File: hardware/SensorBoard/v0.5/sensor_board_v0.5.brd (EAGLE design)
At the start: 46.8 x 39.9 mm, 58 parts, among them J3 USB-MICROB, U1 ATMEGA328P, U2 TSL2561, U4 MPL115A, U5 FT231XS, U6 ADMP401, U7 SHT31-DIS, U8 MCP1703CB, U9 MCP1703CB, Y1 16MHZ

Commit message: Added extra GND vias
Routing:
- net GND: track 76.5 -> 73.8 mm, vias 19 -> 24
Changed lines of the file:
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@@
 </element>
 <element name="C14" library="SparkFun-Passives" package="0805" value="0.1uF" x="32.4612" y="44.1706" smashed="yes">
-<attribute name="VALUE" x="32.1056" y="45.1612" size="0.508" layer="121" font="vector"/>
+<attribute name="VALUE" x="31.496" y="42.8244" size="0.508" layer="121" font="vector"/>
 </element>
 <element name="MICS4514" library="MICS-4514_CO_and_NOx_Sensor_Breakout" package="SPARKFUN-SENSORS_MICS_10-SMD" value="SPARKFUN-SENSORS_MICS-4514" x="28.6512" y="26.4414" smashed="yes" rot="R90">
@@
 <attribute name="MPN" value="" x="27.178" y="44.6024" size="1.778" layer="27" rot="R180" display="off"/>
 <attribute name="OC_NEWARK" value="unknown" x="27.178" y="44.6024" size="1.778" layer="27" rot="R180" display="off"/>
-<attribute name="VALUE" x="28.194" y="43.6626" size="0.508" layer="121" font="vector" rot="R180"/>
+<attribute name="VALUE" x="28.2448" y="43.6626" size="0.508" layer="121" font="vector" rot="R180"/>
 </element>
 <element name="U$4" library="RFM69 USB Gateway" package="LOWPOWERLAB_RFM69W-MINPADS" value="RFM69HW" x="28.8036" y="37.0332" smashed="yes" rot="MR180">
@@
 <wire x1="23.6728" y1="45.0464" x2="23.6596" y2="45.0596" width="0.1778" layer="1"/>
 <wire x1="15.6464" y1="45.0464" x2="15.6464" y2="44.3484" width="0.1778" layer="1"/>
-<wire x1="15.6464" y1="44.3484" x2="17.5768" y2="42.418" width="0.1778" layer="1"/>
 <wire x1="17.5768" y1="42.418" x2="18.3512" y2="42.418" width="0.1778" layer="1"/>
 <wire x1="18.3512" y1="42.418" x2="18.3596" y2="42.4096" width="0.1778" layer="1"/>
@@
 <via x="31.5468" y="42.2148" extent="1-16" drill="0.254" diameter="0.127"/>
 <via x="34.4932" y="45.1612" extent="1-16" drill="0.254" diameter="0.127"/>
-<via x="47.0916" y="44.7548" extent="1-16" drill="0.254" diameter="0.127"/>
+<via x="16.6624" y="42.3672" extent="1-16" drill="0.254" diameter="0.127"/>
 <wire x1="45.2562" y1="28.8504" x2="46.9432" y2="28.8504" width="0.1778" layer="1"/>
 <wire x1="46.9432" y1="28.8504" x2="46.4312" y2="28.6004" width="0.1778" layer="1"/>
@@
 <via x="44.5516" y="33.1978" extent="1-16" drill="0.254" diameter="0.127"/>
 <via x="43.688" y="30.6578" extent="1-16" drill="0.254" diameter="0.127"/>
+<via x="49.9872" y="22.1996" extent="1-16" drill="0.254" diameter="0.127"/>
+<via x="11.938" y="27.3812" extent="1-16" drill="0.254" diameter="0.127"/>
+<via x="29.0576" y="12.5984" extent="1-16" drill="0.254" diameter="0.127"/>
+<via x="32.258" y="23.5204" extent="1-16" drill="0.254" diameter="0.127"/>
+<via x="51.054" y="38.7096" extent="1-16" drill="0.254" diameter="0.127"/>
 </signal>
 <signal name="VCC">

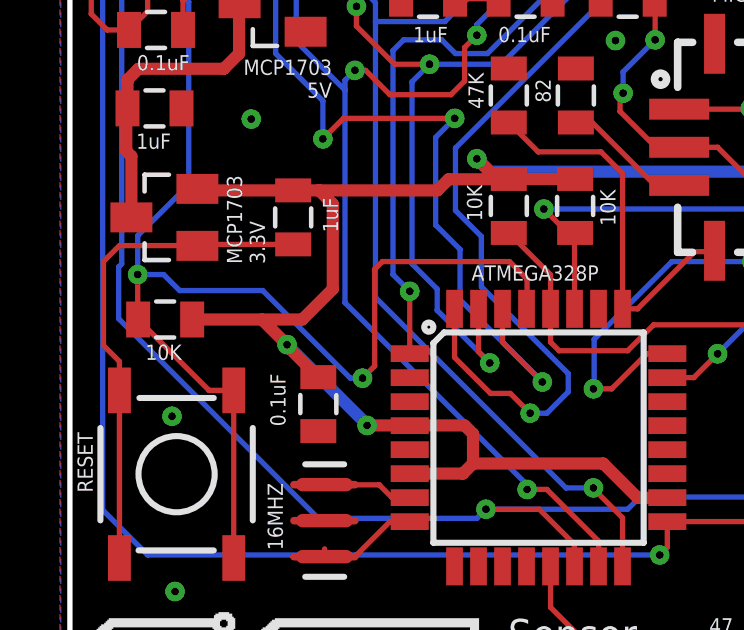
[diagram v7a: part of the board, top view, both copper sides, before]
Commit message: Adjusted some traces around MCU
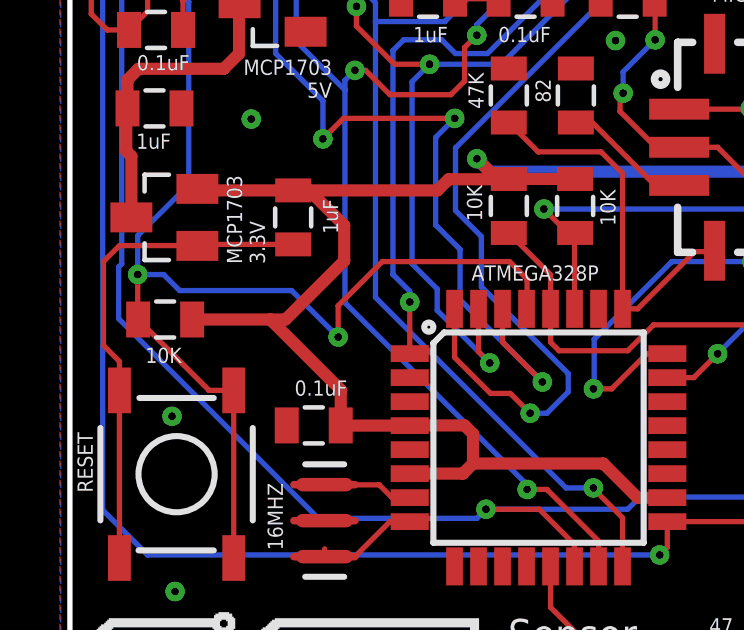
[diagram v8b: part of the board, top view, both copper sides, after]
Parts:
- moved C15 0.73 mm to (14.0, 17.2), turned to 180 degrees
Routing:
- net VCC: track 151.4 -> 148.1 mm, vias 7 -> 5
- net RESET: track 54.9 -> 52.5 mm
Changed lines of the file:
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@@
 <attribute name="MF" value="" x="13.335" y="24.1046" size="1.778" layer="27" rot="R270" display="off"/>
 <attribute name="MPN" value="" x="13.335" y="24.1046" size="1.778" layer="27" rot="R270" display="off"/>
-<attribute name="VALUE" x="14.3256" y="24.765" size="0.508" layer="121" font="vector" rot="R270"/>
+<attribute name="VALUE" x="14.3256" y="24.7142" size="0.508" layer="121" font="vector" rot="R270"/>
 </element>
 <element name="R13" library="SparkFun-Passives" package="0805" value="10K" x="9.0678" y="20.701" smashed="yes">
-<attribute name="VALUE" x="8.4074" y="19.3548" size="0.508" layer="121" font="vector"/>
+<attribute name="VALUE" x="8.4074" y="19.2532" size="0.508" layer="121" font="vector"/>
 </element>
 <element name="C12" library="SparkFun-Passives" package="0805" value="0.1uF" x="8.763" y="30.353" smashed="yes" rot="R180">
@@
 <attribute name="VALUE" x="47.1932" y="50.3936" size="0.8128" layer="27" ratio="10"/>
 </element>
-<element name="C15" library="SparkFun-Passives" package="0805" value="0.1uF" x="14.1732" y="17.8816" smashed="yes" rot="R270">
-<attribute name="VALUE" x="12.573" y="18.8976" size="0.508" layer="121" font="vector" rot="R270"/>
+<element name="C15" library="SparkFun-Passives" package="0805" value="0.1uF" x="14.0208" y="17.1704" smashed="yes" rot="R180">
+<attribute name="VALUE" x="15.1384" y="18.669" size="0.508" layer="121" font="vector" rot="R180"/>
 </element>
 </elements>
@@
 <wire x1="24.8158" y1="14.7574" x2="25.7998" y2="14.7574" width="0.4064" layer="1"/>
 <wire x1="25.7998" y1="14.7574" x2="25.8064" y2="14.764" width="0.1778" layer="1"/>
-<wire x1="9.9678" y1="20.701" x2="12.2936" y2="20.701" width="0.1778" layer="1"/>
-<wire x1="12.2936" y1="20.701" x2="13.1318" y2="19.8628" width="0.4064" layer="1"/>
-<via x="13.1318" y="19.8628" extent="1-16" drill="0.254" diameter="0.127"/>
-<wire x1="17.2276" y1="17.1704" x2="15.7988" y2="17.1704" width="0.4064" layer="1"/>
-<via x="15.7988" y="17.1704" extent="1-16" drill="0.254" diameter="0.127"/>
-<wire x1="15.7988" y1="17.1704" x2="15.7988" y2="17.1958" width="0.1778" layer="16"/>
-<wire x1="15.7988" y1="17.1958" x2="13.1318" y2="19.8628" width="0.4064" layer="16"/>
 <wire x1="10.1924" y1="25.0046" x2="10.1424" y2="25.0546" width="0.1778" layer="1"/>
-<wire x1="13.335" y1="25.0046" x2="14.1986" y2="25.0046" width="0.4064" layer="1"/>
-<wire x1="14.1986" y1="25.0046" x2="18.1466" y2="25.0046" width="0.4064" layer="1"/>
+<wire x1="13.335" y1="25.0046" x2="13.8684" y2="25.0046" width="0.4064" layer="1"/>
+<wire x1="13.8684" y1="25.0046" x2="18.1466" y2="25.0046" width="0.4064" layer="1"/>
 <wire x1="18.1466" y1="25.0046" x2="18.5166" y2="25.3746" width="0.4064" layer="1"/>
 <wire x1="18.5166" y1="25.3746" x2="20.5122" y2="25.3746" width="0.4064" layer="1"/>
 <wire x1="20.5122" y1="25.3746" x2="20.5232" y2="25.3856" width="0.1778" layer="1"/>
-<wire x1="9.9678" y1="20.701" x2="13.6398" y2="20.701" width="0.4064" layer="1"/>
-<wire x1="13.6398" y1="20.701" x2="14.6558" y2="21.717" width="0.4064" layer="1"/>
-<wire x1="14.6558" y1="21.717" x2="14.6558" y2="24.5474" width="0.4064" layer="1"/>
-<wire x1="14.6558" y1="24.5474" x2="14.1986" y2="25.0046" width="0.4064" layer="1"/>
 <via x="39.4462" y="25.6286" extent="1-16" drill="0.254" diameter="0.127"/>
 <wire x1="22.733" y1="25.3856" x2="20.5232" y2="25.3856" width="0.4064" layer="1"/>
@@
 <wire x1="35.306" y1="39.37" x2="35.306" y2="42.2292" width="0.4064" layer="1"/>
 <contactref element="C15" pad="1"/>
-<wire x1="13.1318" y1="19.8628" x2="13.1318" y2="19.823" width="0.4064" layer="1"/>
-<wire x1="13.1318" y1="19.823" x2="14.1732" y2="18.7816" width="0.4064" layer="1"/>
 <wire x1="39.4462" y1="25.6286" x2="39.4462" y2="25.6794" width="0.4064" layer="1"/>
 <wire x1="41.7974" y1="24.7074" x2="41.8306" y2="24.6742" width="0.4064" layer="1"/>
@@
 <wire x1="36.5252" y1="36.6776" x2="36.5252" y2="37.5266" width="0.4064" layer="1"/>
 <wire x1="36.5252" y1="37.5266" x2="36.546" y2="37.5474" width="0.4064" layer="1"/>
+<wire x1="12.573" y1="20.701" x2="14.9352" y2="18.3388" width="0.4064" layer="1"/>
+<wire x1="17.2148" y1="17.1704" x2="17.2212" y2="17.164" width="0.4064" layer="1"/>
+<wire x1="9.9678" y1="20.701" x2="12.573" y2="20.701" width="0.4064" layer="1"/>
+<wire x1="15.0368" y1="22.6568" x2="15.0368" y2="23.8362" width="0.4064" layer="1"/>
+<wire x1="15.0368" y1="23.8362" x2="13.8684" y2="25.0046" width="0.4064" layer="1"/>
+<wire x1="17.2212" y1="17.164" x2="14.9272" y2="17.164" width="0.4064" layer="1"/>
+<wire x1="14.9272" y1="17.164" x2="14.9208" y2="17.1704" width="0.4064" layer="1"/>
+<wire x1="14.9208" y1="17.1704" x2="14.9208" y2="18.3244" width="0.4064" layer="1"/>
+<wire x1="14.9208" y1="18.3244" x2="14.9352" y2="18.3388" width="0.4064" layer="1"/>
+<wire x1="15.0368" y1="22.6568" x2="13.081" y2="20.701" width="0.4064" layer="1"/>
+<wire x1="13.081" y1="20.701" x2="12.573" y2="20.701" width="0.4064" layer="1"/>
 </signal>
 <signal name="SCL">
@@
 <wire x1="8.1534" y1="20.7154" x2="8.1678" y2="20.701" width="0.1778" layer="1"/>
 <wire x1="21.1138" y1="21.0566" x2="21.1138" y2="21.3804" width="0.1778" layer="1"/>
-<wire x1="16.3068" y1="22.6314" x2="16.0528" y2="22.3774" width="0.1778" layer="1"/>
-<wire x1="16.0528" y1="22.3774" x2="16.0528" y2="19.1516" width="0.1778" layer="1"/>
-<wire x1="16.0528" y1="19.1516" x2="15.6464" y2="18.7452" width="0.1778" layer="1"/>
-<via x="15.6464" y="18.7452" extent="1-16" drill="0.254" diameter="0.127"/>
-<wire x1="15.6464" y1="18.7452" x2="15.24" y2="18.7452" width="0.1778" layer="16"/>
-<wire x1="15.24" y1="18.7452" x2="12.319" y2="21.6662" width="0.1778" layer="16"/>
-<wire x1="12.319" y1="21.6662" x2="9.5504" y2="21.6662" width="0.1778" layer="16"/>
+<wire x1="13.2842" y1="21.6662" x2="9.5504" y2="21.6662" width="0.1778" layer="16"/>
 <wire x1="9.5504" y1="21.6662" x2="9.017" y2="22.1996" width="0.1778" layer="16"/>
 <wire x1="9.017" y1="22.1996" x2="8.1534" y2="22.1996" width="0.1778" layer="16"/>
@@
 <wire x1="21.1328" y1="22.0472" x2="21.1328" y2="21.0756" width="0.1778" layer="1"/>
 <wire x1="21.1328" y1="21.0756" x2="21.1138" y2="21.0566" width="0.1778" layer="1"/>
+<wire x1="16.3068" y1="22.6314" x2="14.8336" y2="21.1582" width="0.1778" layer="1"/>
+<wire x1="14.8336" y1="21.1582" x2="14.8336" y2="20.1168" width="0.1778" layer="1"/>
+<via x="14.8336" y="20.1168" extent="1-16" drill="0.254" diameter="0.127"/>
+<wire x1="14.8336" y1="20.1168" x2="13.2842" y2="21.6662" width="0.1778" layer="16"/>
 </signal>
 <signal name="MOSI">
@@
 <contactref element="R20" pad="2"/>
 <contactref element="U1" pad="1"/>
-<wire x1="16.6624" y1="22.1996" x2="17.2212" y2="21.6408" width="0.1778" layer="16"/>
-<via x="17.2212" y="21.6408" extent="1-16" drill="0.254" diameter="0.127"/>
-<wire x1="17.2212" y1="21.6408" x2="17.2212" y2="19.564" width="0.1778" layer="1"/>
 <via x="38.862" y="33.02" extent="1-16" drill="0.254" diameter="0.127"/>
 <wire x1="23.5712" y1="33.3248" x2="19.812" y2="29.5656" width="0.1778" layer="16"/>
@@
 <wire x1="18.288" y1="30.0228" x2="17.018" y2="30.0228" width="0.1778" layer="16"/>
 <wire x1="17.018" y1="30.0228" x2="16.6624" y2="29.6672" width="0.1778" layer="16"/>
+<wire x1="17.2212" y1="19.564" x2="17.2212" y2="21.2852" width="0.1778" layer="1"/>
+<via x="17.2212" y="21.2852" extent="1-16" drill="0.254" diameter="0.127"/>
+<wire x1="17.2212" y1="21.2852" x2="17.2212" y2="21.6408" width="0.1778" layer="16"/>
+<wire x1="17.2212" y1="21.6408" x2="16.6624" y2="22.1996" width="0.1778" layer="16"/>
 </signal>
 <signal name="SS">
